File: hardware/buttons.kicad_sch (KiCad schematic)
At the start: 41 parts, among them SW10 SW_Push, SW11 SW_Push, SW12 SW_Push, SW13 SW_Push, SW14 SW_Push, SW15 SW_Push, SW16 SW_Push, SW17 SW_Push, SW18 SW_Push, SW19 SW_Push, SW20 SW_Push, SW21 SW_Push, SW22 SW_Push, SW23 SW_Push, SW24 SW_Push, SW25 SW_Push, SW26 SW_Push, SW27 SW_Push, SW28 SW_Push, SW29 SW_Push, SW30 SW_Push, SW31 SW_Push, SW32 SW_Push, SW33 SW_Push, SW34 SW_Push, SW35 SW_Push, SW36 SW_Push, SW37 SW_Push, SW38 SW_Push, SW39 SW_Push, SW40 SW_Push, SW41 SW_Push, SW42 SW_Push, SW43 SW_Push, SW44 SW_Push, SW45 SW_Push, SW46 SW_Push, SW47 EC11, SW48 EC11, SW49 EC11, U9 MCP23017_SP

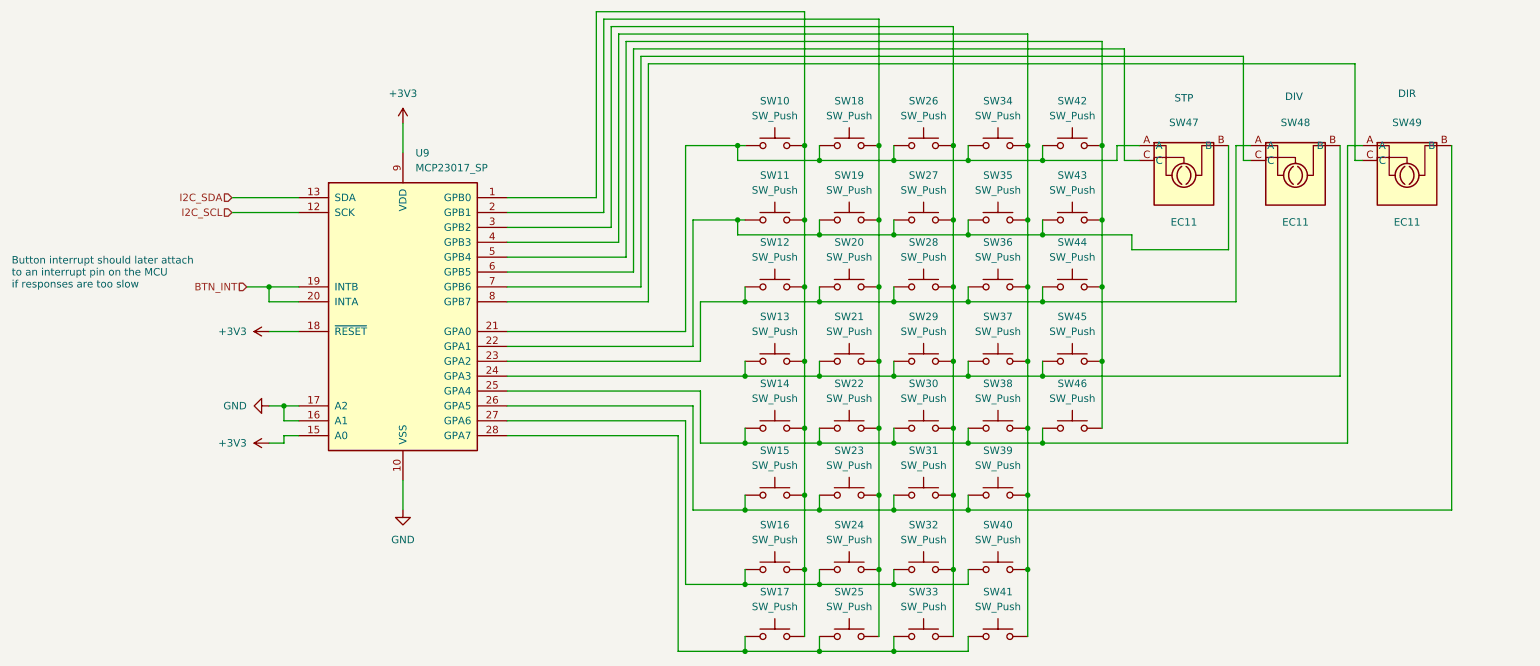
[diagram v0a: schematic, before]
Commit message: Complete hierarchical schematic sheets and fix wiring
- Complete encoder_leds sheet with MAX7219 + 64 LEDs
- Complete ui_leds sheet with MAX7219 + 45 LEDs
- Complete buttons sheet with MCP23017 + 40 buttons
- Complete display sheet with OLED I2C connector
- Complete pots sheet with 3 potentiometers
- Complete encoders sheet with 8 rotary encoders on MCP23017
- Fix inputs sheet hierarchical labels (CLK_IN, RST_IN, SCENE_CV_IN)
- Update MCU sheet with ADC hierarchical labels
- Update root sheet with hierarchical pin connections
- Various ERC fixes and wiring corrections

Co-Authored-By: Claude Opus 4.5 <noreply@anthropic.com>
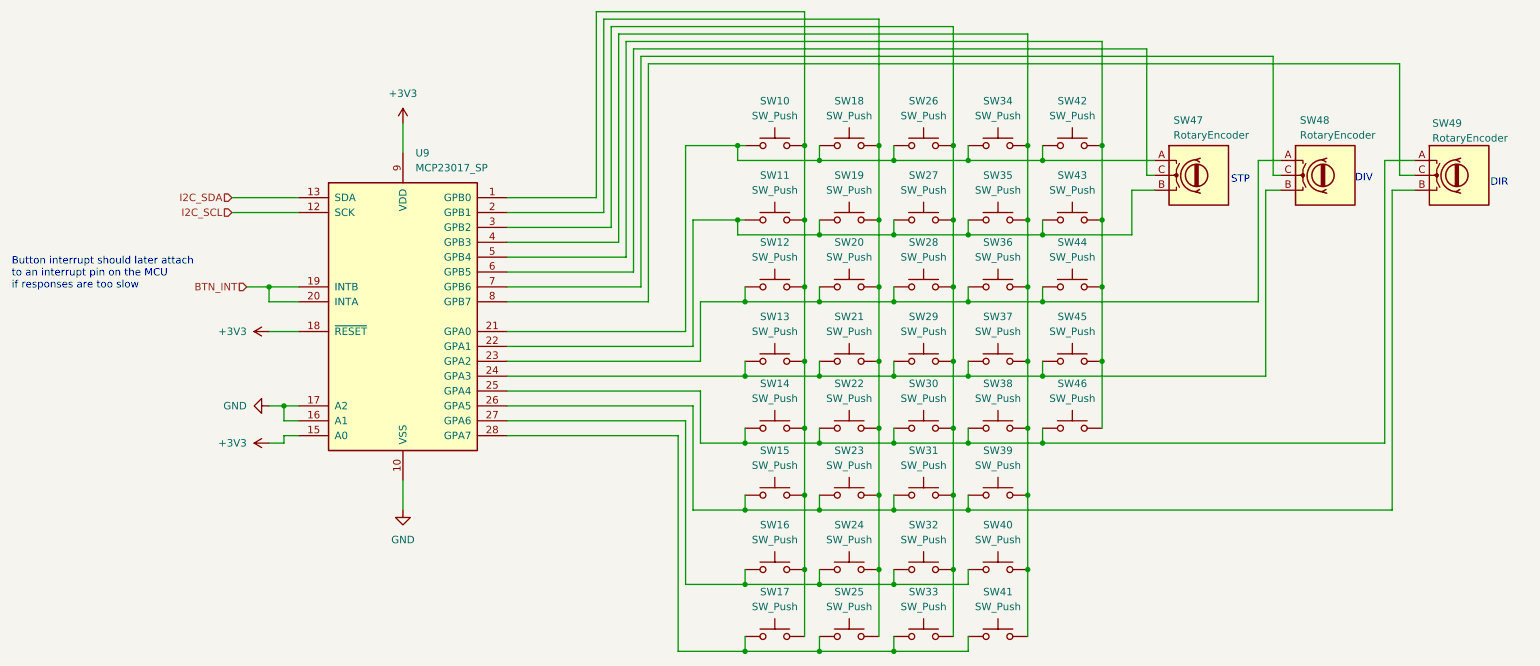
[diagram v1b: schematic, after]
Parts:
- removed SW47, SW48, SW49: EC11, Rotary_Encoder:RotaryEncoder_Alps_EC11E-Switch_Vertical_H20mm, symbol Device:Rotary_Encoder
- added SW47, SW48, SW49: RotaryEncoder, Rotary_Encoder:RotaryEncoder_Alps_EC12E_Vertical_H20mm_CircularMountingHoles, symbol Device:RotaryEncoder
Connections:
- net at SW11.1, SW19.1, SW27.1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: now also SW47.B
- net at SW14.1, SW22.1, SW30.1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: now also SW49.A
- net at SW13.1, SW21.1, SW29.1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: now also SW48.B
- net at SW12.1, SW20.1, SW28.1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: now also SW48.A
- net at SW10.1, SW18.1, SW26.1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: now also SW47.A
- net at SW15.1, SW23.1, SW31.1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: now also SW49.B
- net at U9.6 (GPB5): now also SW47.C
- net at U9.7 (GPB6): now also SW48.C
- net at U9.8 (GPB7): now also SW49.C

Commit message: Assign footprints to all schematic components
SMD footprints assigned:
- Capacitors: 0402 (20pF), 0603 (100nF), 0805 (10uF), 1206 (47uF, 100uF)
- Resistors: 0603
- LEDs: 0201
- MAX7219: SOIC-24W
- ULN2003: SOIC-16
- Switches: TL3342 tactile
- Connectors: JST PH, pin headers

Also removes accidentally committed autosave files.

Co-Authored-By: Claude Opus 4.5 <noreply@anthropic.com>
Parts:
- SW10, SW11, SW12, SW13, SW14, SW15, SW16, SW17, SW18, SW19, SW20, SW21, SW22, SW23, SW24, SW25, SW26, SW27, SW28, SW29, SW30, SW31, SW32, SW33, SW34, SW35, SW36, SW37, SW38, SW39, SW40, SW41, SW42, SW43, SW44, SW45, SW46: footprint Button_Switch_SMD:SW_Push_1P1T_NO_CK_KSC7xxJ -> Button_Switch_THT:SW_PUSH_1P1T_6x3.5mm_H5.0_APEM_MJTP1250
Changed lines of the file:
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@@
 			)
 		)
-		(property "Footprint" "Button_Switch_SMD:SW_Push_1P1T_NO_CK_KSC7xxJ"
+		(property "Footprint" "Button_Switch_THT:SW_PUSH_1P1T_6x3.5mm_H5.0_APEM_MJTP1250"
 			(at 172.72 73.66 0)
 			(effects
@@
 			)
 		)
-		(property "Footprint" "Button_Switch_SMD:SW_Push_1P1T_NO_CK_KSC7xxJ"
+		(property "Footprint" "Button_Switch_THT:SW_PUSH_1P1T_6x3.5mm_H5.0_APEM_MJTP1250"
 			(at 198.12 109.22 0)
 			(effects
@@
 			)
 		)
-		(property "Footprint" "Button_Switch_SMD:SW_Push_1P1T_NO_CK_KSC7xxJ"
+		(property "Footprint" "Button_Switch_THT:SW_PUSH_1P1T_6x3.5mm_H5.0_APEM_MJTP1250"
 			(at 160.02 97.79 0)
 			(effects
@@
 			)
 		)
-		(property "Footprint" "Button_Switch_SMD:SW_Push_1P1T_NO_CK_KSC7xxJ"
+		(property "Footprint" "Button_Switch_THT:SW_PUSH_1P1T_6x3.5mm_H5.0_APEM_MJTP1250"
 			(at 172.72 133.35 0)
 			(effects
@@
 			)
 		)
-		(property "Footprint" "Button_Switch_SMD:SW_Push_1P1T_NO_CK_KSC7xxJ"
+		(property "Footprint" "Button_Switch_THT:SW_PUSH_1P1T_6x3.5mm_H5.0_APEM_MJTP1250"
 			(at 147.32 85.09 0)
 			(effects
@@
 			)
 		)
-		(property "Footprint" "Button_Switch_SMD:SW_Push_1P1T_NO_CK_KSC7xxJ"
+		(property "Footprint" "Button_Switch_THT:SW_PUSH_1P1T_6x3.5mm_H5.0_APEM_MJTP1250"
 			(at 172.72 109.22 0)
 			(effects
@@
 			)
 		)
-		(property "Footprint" "Button_Switch_SMD:SW_Push_1P1T_NO_CK_KSC7xxJ"
+		(property "Footprint" "Button_Switch_THT:SW_PUSH_1P1T_6x3.5mm_H5.0_APEM_MJTP1250"
 			(at 198.12 97.79 0)
 			(effects
@@
 			)
 		)
-		(property "Footprint" "Button_Switch_SMD:SW_Push_1P1T_NO_CK_KSC7xxJ"
+		(property "Footprint" "Button_Switch_THT:SW_PUSH_1P1T_6x3.5mm_H5.0_APEM_MJTP1250"
 			(at 185.42 73.66 0)
 			(effects
@@
 			)
 		)
-		(property "Footprint" "Button_Switch_SMD:SW_Push_1P1T_NO_CK_KSC7xxJ"
+		(property "Footprint" "Button_Switch_THT:SW_PUSH_1P1T_6x3.5mm_H5.0_APEM_MJTP1250"
 			(at 172.72 85.09 0)
 			(effects
@@
 			)
 		)
-		(property "Footprint" "Button_Switch_SMD:SW_Push_1P1T_NO_CK_KSC7xxJ"
+		(property "Footprint" "Button_Switch_THT:SW_PUSH_1P1T_6x3.5mm_H5.0_APEM_MJTP1250"
 			(at 160.02 144.78 0)
 			(effects
@@
 			)
 		)
-		(property "Footprint" "Button_Switch_SMD:SW_Push_1P1T_NO_CK_KSC7xxJ"
+		(property "Footprint" "Button_Switch_THT:SW_PUSH_1P1T_6x3.5mm_H5.0_APEM_MJTP1250"
 			(at 172.72 60.96 0)
 			(effects
@@
 			)
 		)
-		(property "Footprint" "Button_Switch_SMD:SW_Push_1P1T_NO_CK_KSC7xxJ"
+		(property "Footprint" "Button_Switch_THT:SW_PUSH_1P1T_6x3.5mm_H5.0_APEM_MJTP1250"
 			(at 185.42 97.79 0)
 			(effects
@@
 			)
 		)
-		(property "Footprint" "Button_Switch_SMD:SW_Push_1P1T_NO_CK_KSC7xxJ"
+		(property "Footprint" "Button_Switch_THT:SW_PUSH_1P1T_6x3.5mm_H5.0_APEM_MJTP1250"
 			(at 147.32 133.35 0)
 			(effects
@@
 			)
 		)
-		(property "Footprint" "Button_Switch_SMD:SW_Push_1P1T_NO_CK_KSC7xxJ"
+		(property "Footprint" "Button_Switch_THT:SW_PUSH_1P1T_6x3.5mm_H5.0_APEM_MJTP1250"
 			(at 185.42 60.96 0)
 			(effects
@@
 			)
 		)
-		(property "Footprint" "Button_Switch_SMD:SW_Push_1P1T_NO_CK_KSC7xxJ"
+		(property "Footprint" "Button_Switch_THT:SW_PUSH_1P1T_6x3.5mm_H5.0_APEM_MJTP1250"
 			(at 160.02 85.09 0)
 			(effects
@@
 			)
 		)
-		(property "Footprint" "Button_Switch_SMD:SW_Push_1P1T_NO_CK_KSC7xxJ"
+		(property "Footprint" "Button_Switch_THT:SW_PUSH_1P1T_6x3.5mm_H5.0_APEM_MJTP1250"
 			(at 185.42 120.65 0)
 			(effects
@@
 			)
 		)
-		(property "Footprint" "Button_Switch_SMD:SW_Push_1P1T_NO_CK_KSC7xxJ"
+		(property "Footprint" "Button_Switch_THT:SW_PUSH_1P1T_6x3.5mm_H5.0_APEM_MJTP1250"
 			(at 172.72 120.65 0)
 			(effects
@@
 			)
 		)
-		(property "Footprint" "Button_Switch_SMD:SW_Push_1P1T_NO_CK_KSC7xxJ"
+		(property "Footprint" "Button_Switch_THT:SW_PUSH_1P1T_6x3.5mm_H5.0_APEM_MJTP1250"
 			(at 185.42 109.22 0)
 			(effects
@@
 			)
 		)
-		(property "Footprint" "Button_Switch_SMD:SW_Push_1P1T_NO_CK_KSC7xxJ"
+		(property "Footprint" "Button_Switch_THT:SW_PUSH_1P1T_6x3.5mm_H5.0_APEM_MJTP1250"
 			(at 160.02 109.22 0)
 			(effects
@@
 			)
 		)
-		(property "Footprint" "Button_Switch_SMD:SW_Push_1P1T_NO_CK_KSC7xxJ"
+		(property "Footprint" "Button_Switch_THT:SW_PUSH_1P1T_6x3.5mm_H5.0_APEM_MJTP1250"
 			(at 147.32 73.66 0)
 			(effects
@@
 			)
 		)
-		(property "Footprint" "Button_Switch_SMD:SW_Push_1P1T_NO_CK_KSC7xxJ"
+		(property "Footprint" "Button_Switch_THT:SW_PUSH_1P1T_6x3.5mm_H5.0_APEM_MJTP1250"
 			(at 147.32 120.65 0)
 			(effects
@@
 			)
 		)
-		(property "Footprint" "Button_Switch_SMD:SW_Push_1P1T_NO_CK_KSC7xxJ"
+		(property "Footprint" "Button_Switch_THT:SW_PUSH_1P1T_6x3.5mm_H5.0_APEM_MJTP1250"
 			(at 147.32 97.79 0)
 			(effects
@@
 			)
 		)
-		(property "Footprint" "Button_Switch_SMD:SW_Push_1P1T_NO_CK_KSC7xxJ"
+		(property "Footprint" "Button_Switch_THT:SW_PUSH_1P1T_6x3.5mm_H5.0_APEM_MJTP1250"
 			(at 198.12 85.09 0)
 			(effects
@@
 			)
 		)
-		(property "Footprint" "Button_Switch_SMD:SW_Push_1P1T_NO_CK_KSC7xxJ"
+		(property "Footprint" "Button_Switch_THT:SW_PUSH_1P1T_6x3.5mm_H5.0_APEM_MJTP1250"
 			(at 147.32 60.96 0)
 			(effects
@@
 			)
 		)
-		(property "Footprint" "Button_Switch_SMD:SW_Push_1P1T_NO_CK_KSC7xxJ"
+		(property "Footprint" "Button_Switch_THT:SW_PUSH_1P1T_6x3.5mm_H5.0_APEM_MJTP1250"
 			(at 147.32 144.78 0)
 			(effects
@@
 			)
 		)
-		(property "Footprint" "Button_Switch_SMD:SW_Push_1P1T_NO_CK_KSC7xxJ"
+		(property "Footprint" "Button_Switch_THT:SW_PUSH_1P1T_6x3.5mm_H5.0_APEM_MJTP1250"
 			(at 185.42 133.35 0)
 			(effects
@@
 			)
 		)
-		(property "Footprint" "Button_Switch_SMD:SW_Push_1P1T_NO_CK_KSC7xxJ"
+		(property "Footprint" "Button_Switch_THT:SW_PUSH_1P1T_6x3.5mm_H5.0_APEM_MJTP1250"
 			(at 198.12 60.96 0)
 			(effects
@@
 			)
 		)
-		(property "Footprint" "Button_Switch_SMD:SW_Push_1P1T_NO_CK_KSC7xxJ"
+		(property "Footprint" "Button_Switch_THT:SW_PUSH_1P1T_6x3.5mm_H5.0_APEM_MJTP1250"
 			(at 160.02 60.96 0)
 			(effects
@@
 			)
 		)
-		(property "Footprint" "Button_Switch_SMD:SW_Push_1P1T_NO_CK_KSC7xxJ"
+		(property "Footprint" "Button_Switch_THT:SW_PUSH_1P1T_6x3.5mm_H5.0_APEM_MJTP1250"
 			(at 160.02 133.35 0)
 			(effects
@@
 			)
 		)
-		(property "Footprint" "Button_Switch_SMD:SW_Push_1P1T_NO_CK_KSC7xxJ"
+		(property "Footprint" "Button_Switch_THT:SW_PUSH_1P1T_6x3.5mm_H5.0_APEM_MJTP1250"
 			(at 160.02 73.66 0)
 			(effects
@@
 			)
 		)
-		(property "Footprint" "Button_Switch_SMD:SW_Push_1P1T_NO_CK_KSC7xxJ"
+		(property "Footprint" "Button_Switch_THT:SW_PUSH_1P1T_6x3.5mm_H5.0_APEM_MJTP1250"
 			(at 185.42 144.78 0)
 			(effects
@@
 			)
 		)
-		(property "Footprint" "Button_Switch_SMD:SW_Push_1P1T_NO_CK_KSC7xxJ"
+		(property "Footprint" "Button_Switch_THT:SW_PUSH_1P1T_6x3.5mm_H5.0_APEM_MJTP1250"
 			(at 147.32 109.22 0)
 			(effects
@@
 			)
 		)
-		(property "Footprint" "Button_Switch_SMD:SW_Push_1P1T_NO_CK_KSC7xxJ"
+		(property "Footprint" "Button_Switch_THT:SW_PUSH_1P1T_6x3.5mm_H5.0_APEM_MJTP1250"
 			(at 172.72 144.78 0)
 			(effects
@@
 			)
 		)
-		(property "Footprint" "Button_Switch_SMD:SW_Push_1P1T_NO_CK_KSC7xxJ"
+		(property "Footprint" "Button_Switch_THT:SW_PUSH_1P1T_6x3.5mm_H5.0_APEM_MJTP1250"
 			(at 198.12 73.66 0)
 			(effects
@@
 			)
 		)
-		(property "Footprint" "Button_Switch_SMD:SW_Push_1P1T_NO_CK_KSC7xxJ"
+		(property "Footprint" "Button_Switch_THT:SW_PUSH_1P1T_6x3.5mm_H5.0_APEM_MJTP1250"
 			(at 185.42 85.09 0)
 			(effects
@@
 			)
 		)
-		(property "Footprint" "Button_Switch_SMD:SW_Push_1P1T_NO_CK_KSC7xxJ"
+		(property "Footprint" "Button_Switch_THT:SW_PUSH_1P1T_6x3.5mm_H5.0_APEM_MJTP1250"
 			(at 172.72 97.79 0)
 			(effects
@@
 			)
 		)
-		(property "Footprint" "Button_Switch_SMD:SW_Push_1P1T_NO_CK_KSC7xxJ"
+		(property "Footprint" "Button_Switch_THT:SW_PUSH_1P1T_6x3.5mm_H5.0_APEM_MJTP1250"
 			(at 160.02 120.65 0)
 			(effects
